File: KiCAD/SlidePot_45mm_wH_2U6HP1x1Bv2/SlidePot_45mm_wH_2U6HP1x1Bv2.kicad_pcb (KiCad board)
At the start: 2 copper layers, 30 x 84 mm, 4 parts

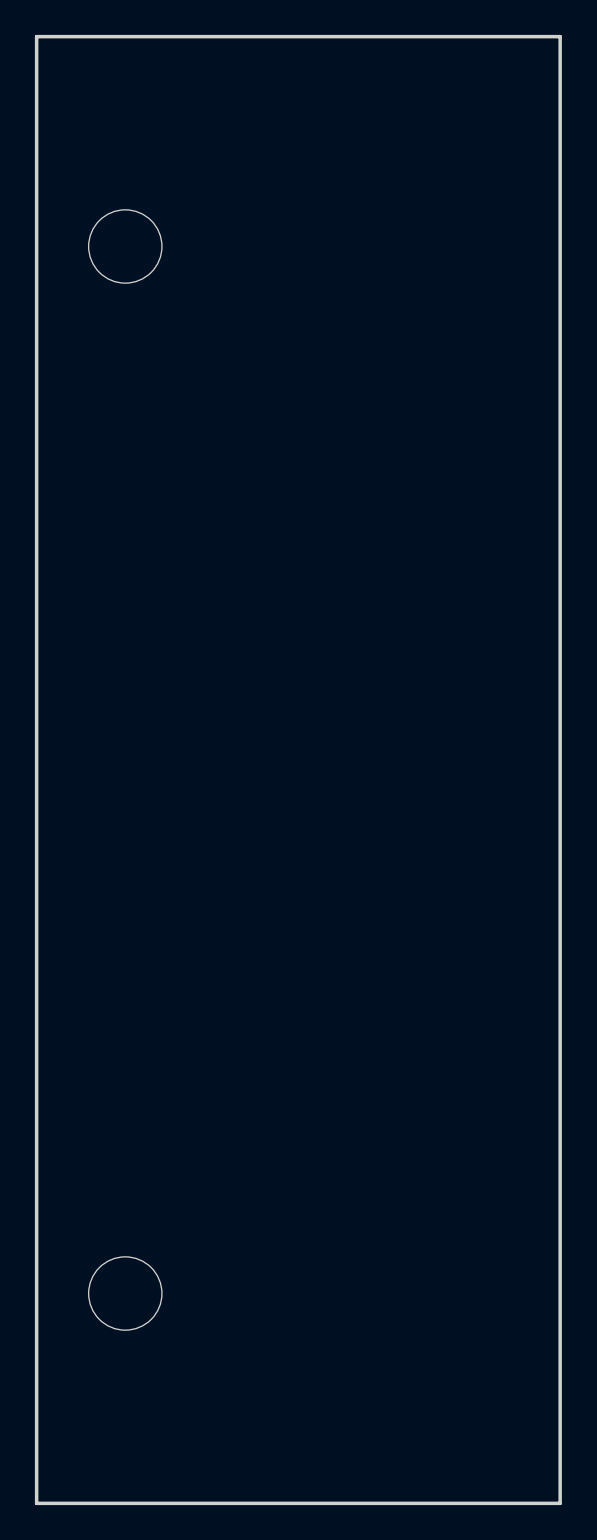
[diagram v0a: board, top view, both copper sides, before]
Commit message: updated all modules to use plated through-holes wherever possible
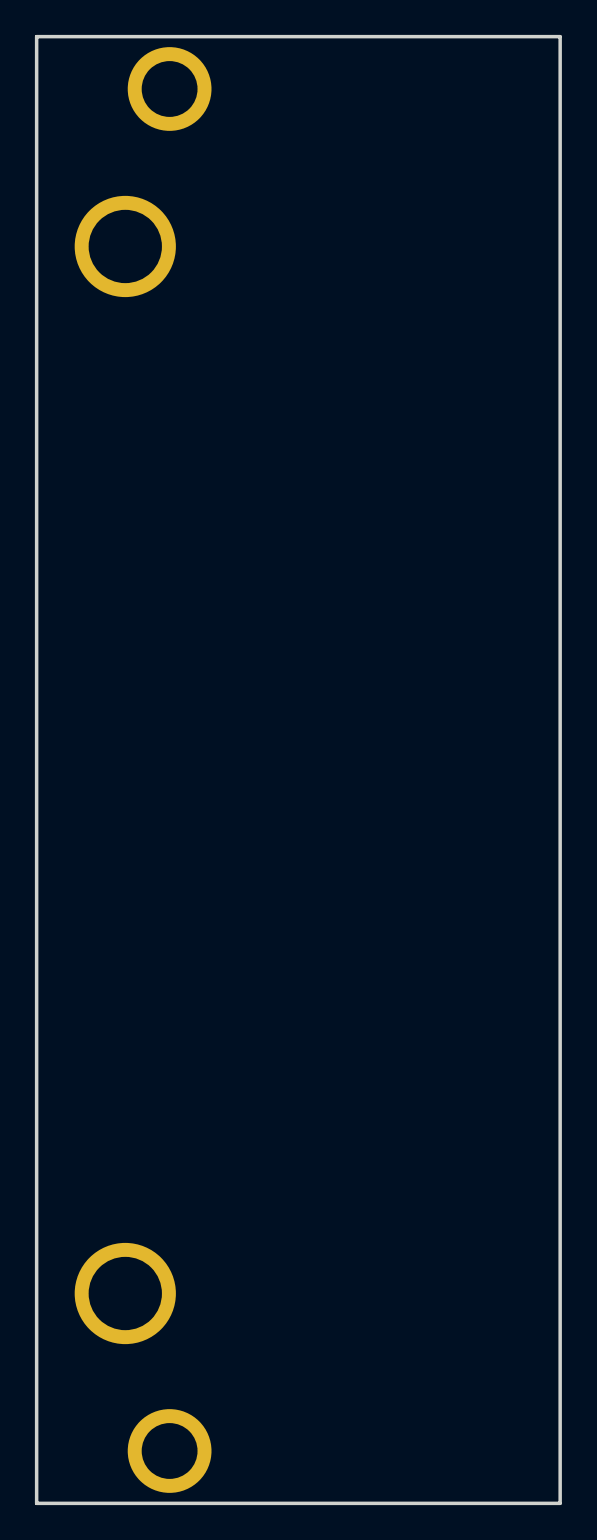
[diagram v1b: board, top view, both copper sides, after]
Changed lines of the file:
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@@
 			)
 		)
-		(pad "" np_thru_hole circle
+		(pad "" thru_hole circle
 			(at 0 0)
-			(size 4.2 4.2)
+			(size 5.8 5.8)
 			(drill 4.2)
 			(layers "*.Cu" "*.Mask")
-		)
-		(pad "" np_thru_hole circle
+			(remove_unused_layers no)
+		)
+		(pad "" thru_hole circle
 			(at 0 60)
-			(size 4.2 4.2)
+			(size 5.8 5.8)
 			(drill 4.2)
 			(layers "*.Cu" "*.Mask")
+			(remove_unused_layers no)
 		)
 		(embedded_fonts no)
@@
 			)
 		)
-		(pad "" np_thru_hole oval
+		(pad "" thru_hole circle
 			(at 0 0)
-			(size 4.34 3.2)
-			(drill oval 4.34 3.2)
+			(size 4.8 4.8)
+			(drill 3.2)
 			(layers "*.Cu" "*.Mask")
+			(remove_unused_layers no)
 		)
 		(embedded_fonts no)
@@
 			)
 		)
-		(pad "" np_thru_hole oval
+		(pad "" thru_hole circle
 			(at 0 0)
-			(size 4.34 3.2)
-			(drill oval 4.34 3.2)
+			(size 4.8 4.8)
+			(drill 3.2)
 			(layers "*.Cu" "*.Mask")
+			(remove_unused_layers no)
 		)
 		(embedded_fonts no)
